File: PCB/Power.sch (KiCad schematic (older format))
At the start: 18 parts, among them J1 B2B-PH-K-S(LF)(SN), J2 B3B-PH-K-S(LF)(SN), Q1 DMG2307L-7, Q2 DMG2307L-7, U1 BQ24210DQCT, U2 AZ1117CR-3.3TRG1_1

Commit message: On/Off And Cleanup
Onoff Switch added, PCB extended 1mm to accomodated everything. routing
and traes cleaned up. Heat sinking ground pours added to the BQ chip
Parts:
- added SW3: CUS-12TB, PCB_Footprints:CUS-12TB, symbol CUS-12TB
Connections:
- wire segments 41 -> 56
- no-connect marks 0 -> 1
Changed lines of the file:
@@
 $EndComp
 Wire Wire Line
-	800  2575 7775 2575
-Wire Wire Line
-	2200 2575 2200 3400
-Wire Wire Line
-	2200 2900 4675 2900
-Wire Wire Line
-	5775 2900 7675 2900
+	800  2575 2200 2575
+Wire Wire Line
+	2200 2575 7500 2575
+Wire Wire Line
+	7500 2575 7775 2575
+Wire Wire Line
+	2200 2575 2200 2900
+Wire Wire Line
+	2200 2900 2200 3400
+Wire Wire Line
+	2200 2900 3500 2900
+Wire Wire Line
+	3500 2900 4100 2900
+Wire Wire Line
+	4100 2900 4675 2900
+Wire Wire Line
+	5775 2900 6900 2900
+Wire Wire Line
+	6900 2900 7100 2900
+Wire Wire Line
+	7100 2900 7275 2900
+Wire Wire Line
+	7275 2900 7675 2900
 Wire Wire Line
 	8275 2575 8275 2900
@@
 Connection ~ 7500 2575
 Wire Wire Line
-	8275 2900 9100 2900
-Wire Wire Line
-	10100 2900 10875 2900
+	8275 2900 8900 2900
+Wire Wire Line
+	8900 2900 9100 2900
+Wire Wire Line
+	10100 2900 10325 2900
+Wire Wire Line
+	10325 2900 10875 2900
 Connection ~ 10325 2900
 $Comp
-L +3.3V #PWR35
+L +3.3V #PWR36
 U 1 1 57D80E79
 P 10875 2900
-F 0 "#PWR35" H 10875 2750 50  0001 C CNN
+F 0 "#PWR36" H 10875 2750 50  0001 C CNN
 F 1 "+3.3V" H 10875 3040 50  0000 C CNN
 F 2 "" H 10875 2900 50  0000 C CNN
@@
 $EndComp
 $Comp
-L GND #PWR34
+L GND #PWR35
 U 1 1 57D80F19
 P 9600 3350
-F 0 "#PWR34" H 9600 3100 50  0001 C CNN
+F 0 "#PWR35" H 9600 3100 50  0001 C CNN
 F 1 "GND" H 9600 3200 50  0000 C CNN
 F 2 "" H 9600 3350 50  0000 C CNN
@@
 $EndComp
 Wire Wire Line
-	8900 3350 10325 3350
+	8900 3350 9600 3350
+Wire Wire Line
+	9600 3350 10325 3350
 Connection ~ 9600 3350
 Connection ~ 8900 2900
@@
 	5775 3200 6000 3200
 Wire Wire Line
-	6000 3200 6000 4875
+	6000 3200 6000 3325
+Wire Wire Line
+	6000 3325 6000 4875
 Wire Wire Line
 	6000 4875 4675 4875
@@
 Connection ~ 6000 3325
 $Comp
-L GND #PWR32
+L GND #PWR33
 U 1 1 57D82F5E
 P 5225 4600
-F 0 "#PWR32" H 5225 4350 50  0001 C CNN
+F 0 "#PWR33" H 5225 4350 50  0001 C CNN
 F 1 "GND" H 5225 4450 50  0000 C CNN
 F 2 "" H 5225 4600 50  0000 C CNN
@@
 	5225 4000 5225 4600
 Wire Wire Line
-	5125 4600 5325 4600
+	5125 4600 5225 4600
+Wire Wire Line
+	5225 4600 5325 4600
 Wire Wire Line
 	5325 4600 5325 4000
@@
 $EndComp
 $Comp
-L GND #PWR31
+L GND #PWR32
 U 1 1 57D853F5
 P 4100 3350
-F 0 "#PWR31" H 4100 3100 50  0001 C CNN
+F 0 "#PWR32" H 4100 3100 50  0001 C CNN
 F 1 "GND" H 4100 3200 50  0000 C CNN
 F 2 "" H 4100 3350 50  0000 C CNN
@@
 	1925 4050 2725 4050
 Wire Wire Line
-	1925 3975 2725 3975
-Text Label 2075 3975 0    60   ~ 0
+	1925 3975 3150 3975
+Text Label 2975 3875 0    60   ~ 0
 BAT
 Text Label 2075 4050 0    60   ~ 0
@@
 $EndComp
 $Comp
-L GND #PWR33
+L GND #PWR34
 U 1 1 57E05471
 P 8775 4525
-F 0 "#PWR33" H 8775 4275 50  0001 C CNN
+F 0 "#PWR34" H 8775 4275 50  0001 C CNN
 F 1 "GND" H 8775 4375 50  0000 C CNN
 F 2 "" H 8775 4525 50  0000 C CNN
@@
 	8775 4225 8775 4525
 Wire Wire Line
-	7975 4225 8175 4225
+	7975 4225 8100 4225
+Wire Wire Line
+	8100 4225 8175 4225
 Wire Wire Line
 	8100 4225 8100 5200
@@
 Text HLabel 975  5200 0    60   Output ~ 0
 BAT_VOLT
+NoConn ~ 3150 4075
+$Comp
+L CUS-12TB SW3
+U 1 1 580F4884
+P 3425 3975
+F 0 "SW3" V 3422 3697 60  0000 R CNN
+F 1 "CUS-12TB" V 3316 3697 60  0000 R CNN
+F 2 "PCB_Footprints:CUS-12TB" H 2675 4950 60  0001 C CNN
+F 3 "http://www.nidec-copal-electronics.com/e/catalog/switch/cus.pdf" H 2775 5050 60  0001 C CNN
+F 4 "0.45329 @ 1000" H 2875 5150 60  0001 C CNN "Cost"
+F 5 "24 Oct 2016" H 2975 5250 60  0001 C CNN "Date Created"
+F 6 "24 Oct 2016" H 3075 5350 60  0001 C CNN "Date Modifed"
+F 7 "Adam Vadala-Roth" H 3175 5450 60  0001 C CNN "Designer"
+F 8 "2mm" H 3275 5550 60  0001 C CNN "Height"
+F 9 "Yes" H 3375 5650 60  0001 C CNN "RHoS?"
+F 10 "Copal Electronics Inc." H 3475 5750 60  0001 C CNN "MFR"
+F 11 "CUS-12TB" H 3575 5850 60  0001 C CNN "MFR#"
+F 12 "SMT/SMD" H 3675 5950 60  0001 C CNN "Mounting"
+F 13 "3" H 3775 6050 60  0001 C CNN "Pin Count#"
+F 14 "Active" H 3875 6150 60  0001 C CNN "Status"
+F 15 "N/A" H 3975 6250 60  0001 C CNN "Tolerance"
+F 16 "SMT Slider switch SPDT" H 4075 6350 60  0001 C CNN "Type"
+F 17 "50V 100mA" H 4175 6450 60  0001 C CNN "Voltage"
+F 18 "N/A" H 4725 6450 60  0001 C CNN "Wattage"
+F 19 "N/A" H 3125 4850 60  0001 C CNN "Componen-Value"
+F 20 "Slide Switch SPDT Surface Mount, Right Angle" H 4925 6650 60  0001 C CNN "Description"
+	1    3425 3975
+	0    -1   -1   0
+$EndComp
+$Comp
+L GND #PWR31
+U 1 1 580F4AAD
+P 3425 4375
+F 0 "#PWR31" H 3425 4125 50  0001 C CNN
+F 1 "GND" H 3425 4225 50  0000 C CNN
+F 2 "" H 3425 4375 50  0000 C CNN
+F 3 "" H 3425 4375 50  0000 C CNN
+	1    3425 4375
+	1    0    0    -1
+$EndComp
+Wire Wire Line
+	3150 3875 2875 3875
 $EndSCHEMATC

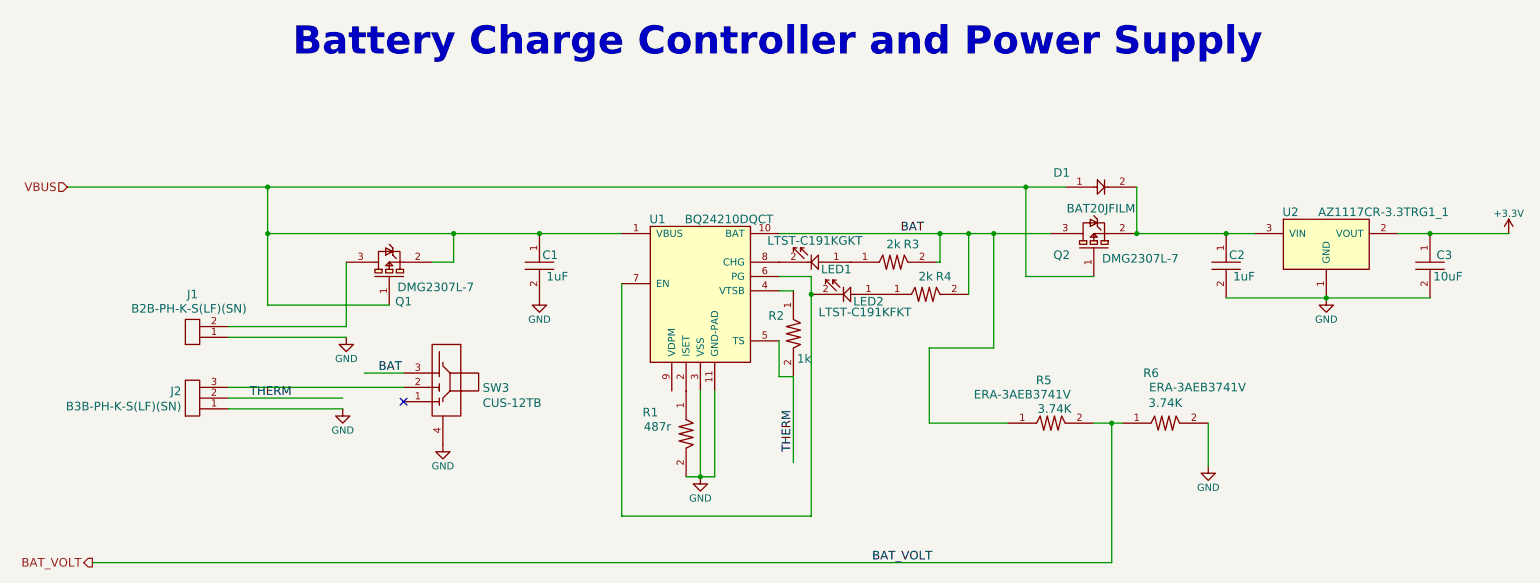
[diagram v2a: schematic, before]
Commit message: New Power Topology
LDO swapped for one with a shutdown enable from Microchip. On/Off
switchnow toggles the shutdown enable from the new LDO.
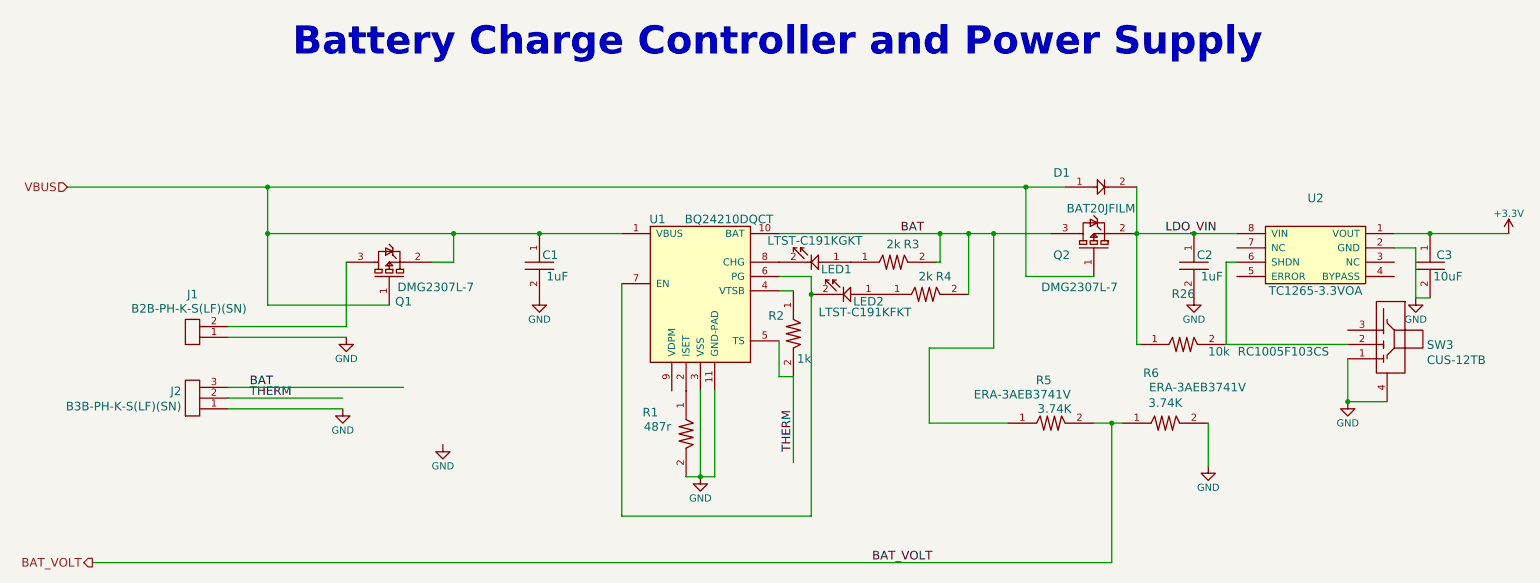
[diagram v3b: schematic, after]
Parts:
- removed U2: AZ1117CR-3.3TRG1_1, PCB_Footprints:AZ1117CR-3.3TRG1, symbol AZ1117CR-3.3TRG1_1
- added R26: RC1005F103CS, PCB_Footprints:R0402, symbol RC1005F103CS
- added U2: TC1265-3.3VOA, PCB_Footprints:TC1265-3.3VOA, symbol TC1265-3.3VOA
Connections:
- net labels added: LDO_VIN
- wire segments 56 -> 50
- no-connect marks 1 -> 0
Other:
- moved on the sheet: C2, SW3
